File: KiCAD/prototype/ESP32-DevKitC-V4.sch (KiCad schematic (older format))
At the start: 10 parts

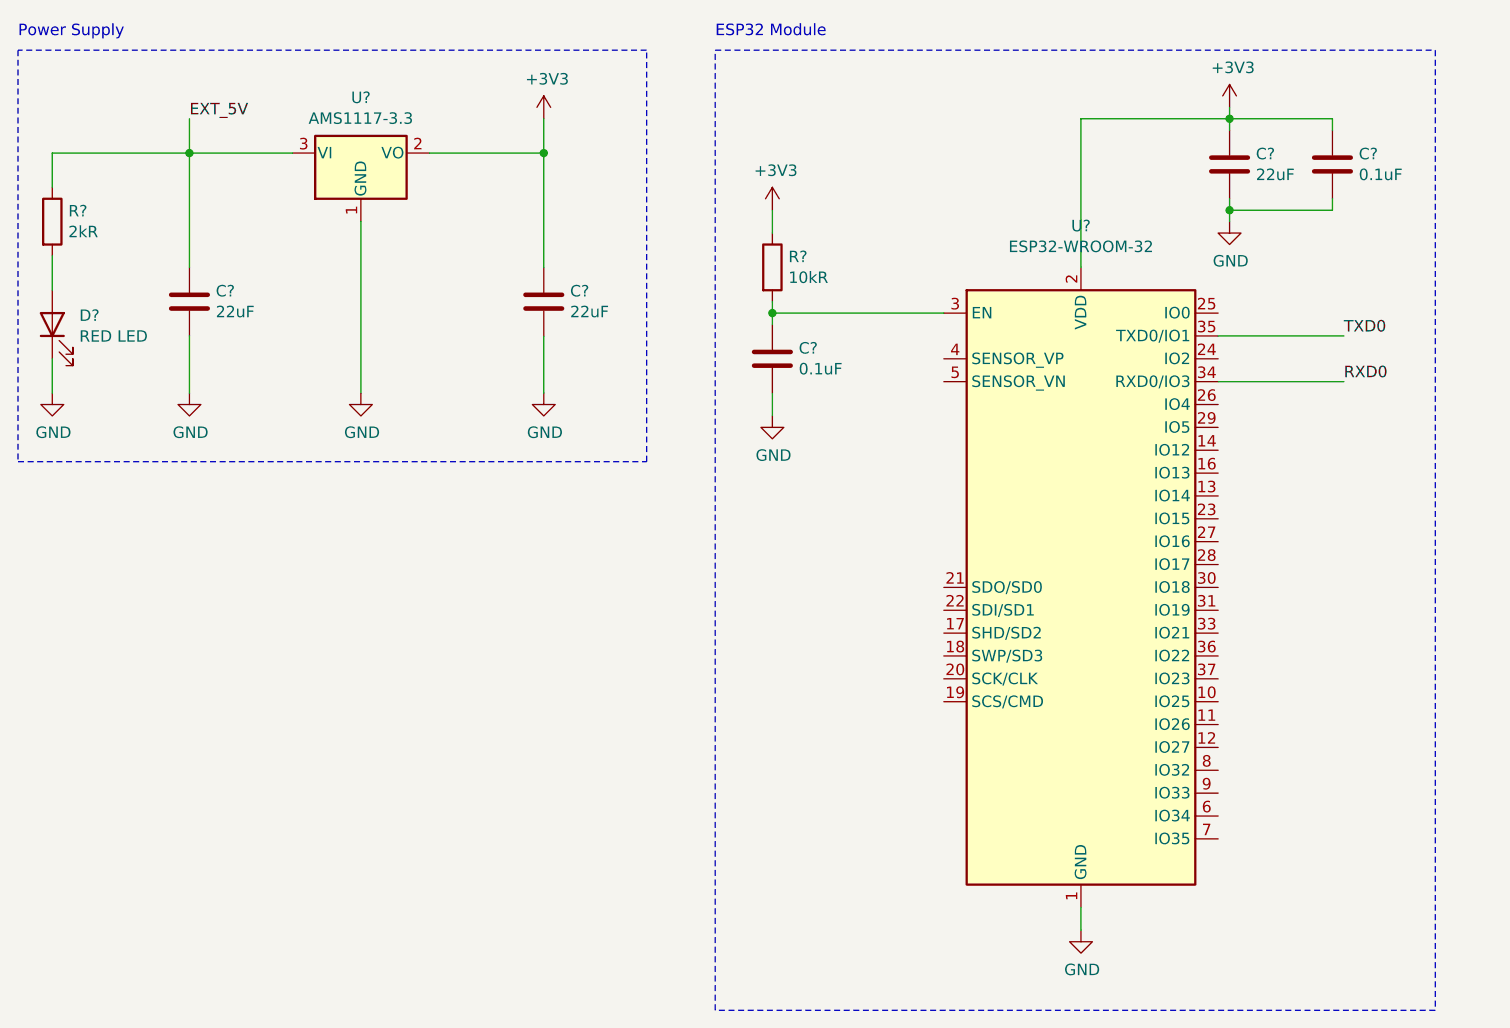
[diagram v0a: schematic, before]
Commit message: Add switch button connections
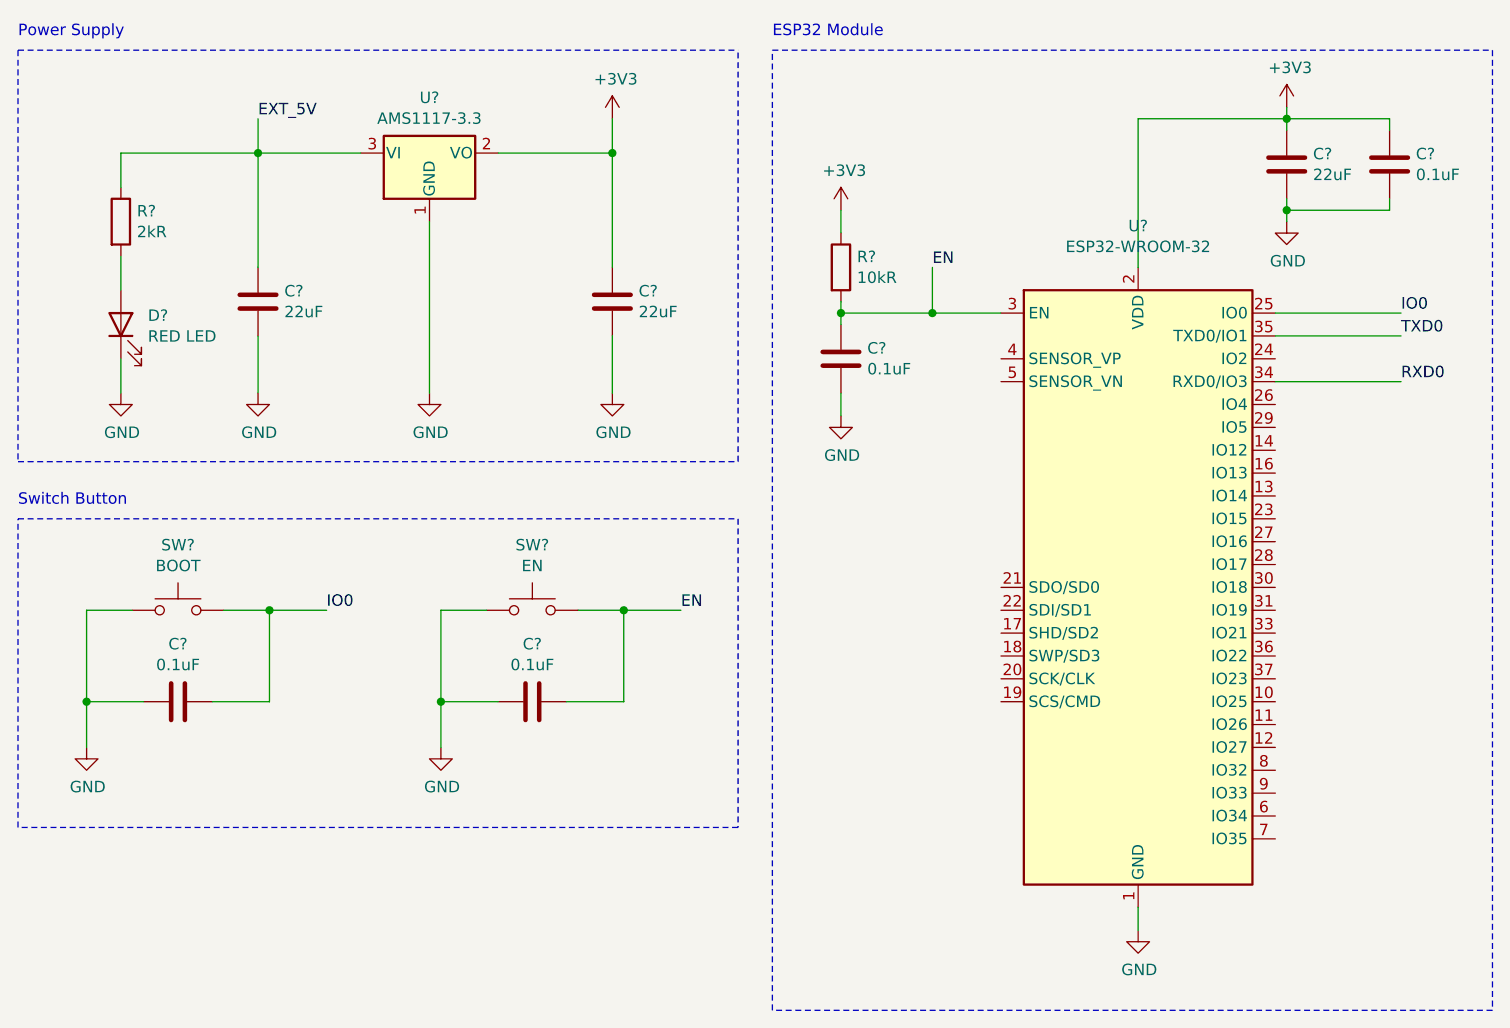
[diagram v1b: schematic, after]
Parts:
- added C? (x2): 0.1uF, symbol Device:C
- added SW?: BOOT, symbol Switch:SW_Push
- added SW?: EN, symbol Switch:SW_Push
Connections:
- net GND: now also C?.1, C?.1, SW?.1, SW?.1
- net IO0: now reaches U?.25 (IO0)
- net IO0: now also C?.2, SW?.2
- net EN: now reaches C?.1, R?.2, U?.3 (EN)
- net EN: now also C?.2, SW?.2
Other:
- note added: "Switch Button"
- moved on the sheet: C?, D?, R?, U?

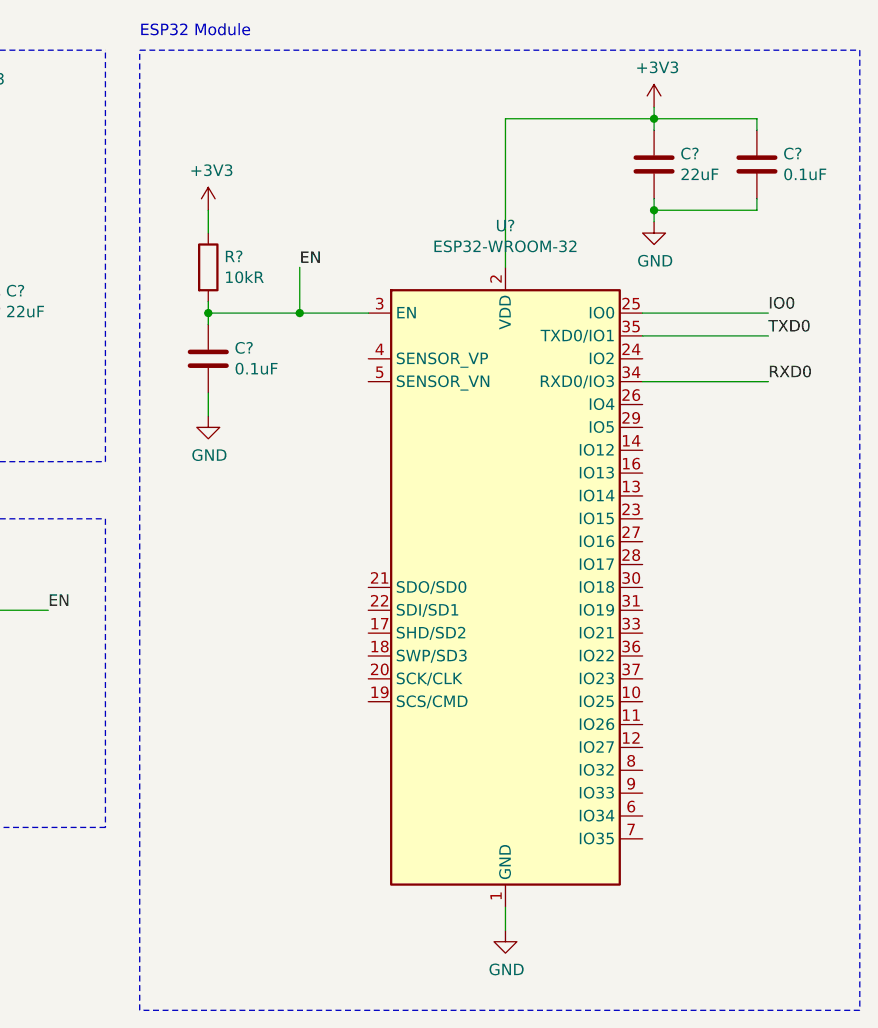
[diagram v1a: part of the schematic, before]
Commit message: Finish labels on ESP32 module
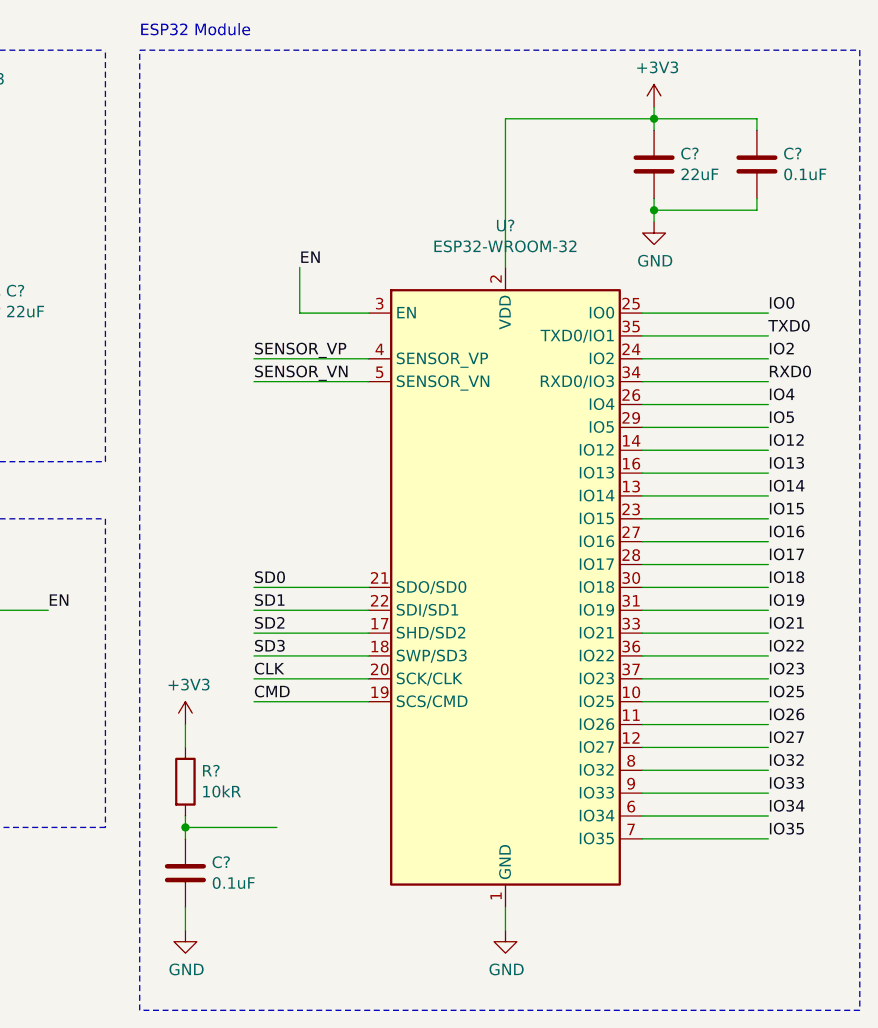
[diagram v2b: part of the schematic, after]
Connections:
- net EN: no longer C?.1, R?.2
- net IO25: now reaches U?.10 (IO25)
- net IO26: now reaches U?.11 (IO26)
- net IO27: now reaches U?.12 (IO27)
- net IO14: now reaches U?.13 (IO14)
- net IO12: now reaches U?.14 (IO12)
- net IO13: now reaches U?.16 (IO13)
- net SD2: now reaches U?.17 (SHD/SD2)
- net SD3: now reaches U?.18 (SWP/SD3)
- net CMD: now reaches U?.19 (SCS/CMD)
- net CLK: now reaches U?.20 (SCK/CLK)
- net SD0: now reaches U?.21 (SDO/SD0)
- net SD1: now reaches U?.22 (SDI/SD1)
- net IO15: now reaches U?.23 (IO15)
- net IO2: now reaches U?.24 (IO2)
- net IO4: now reaches U?.26 (IO4)
- net IO16: now reaches U?.27 (IO16)
- net IO17: now reaches U?.28 (IO17)
- net IO5: now reaches U?.29 (IO5)
- net IO18: now reaches U?.30 (IO18)
- net IO19: now reaches U?.31 (IO19)
- net IO21: now reaches U?.33 (IO21)
- net IO22: now reaches U?.36 (IO22)
- net IO23: now reaches U?.37 (IO23)
- net SENSOR_VP: now reaches U?.4 (SENSOR_VP)
- net SENSOR_VN: now reaches U?.5 (SENSOR_VN)
- net IO34: now reaches U?.6 (IO34)
- net IO35: now reaches U?.7 (IO35)
- net IO32: now reaches U?.8 (IO32)
- net IO33: now reaches U?.9 (IO33)
- new net: C?.1, R?.2
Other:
- moved on the sheet: C?, R?
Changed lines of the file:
@@
 L power:+3V3 #PWR?
 U 1 1 5F9419AA
-P 4300 1400
-F 0 "#PWR?" H 4300 1250 50  0001 C CNN
-F 1 "+3V3" H 4315 1573 50  0000 C CNN
-F 2 "" H 4300 1400 50  0001 C CNN
-F 3 "" H 4300 1400 50  0001 C CNN
-	1    4300 1400
+P 4200 3650
+F 0 "#PWR?" H 4200 3500 50  0001 C CNN
+F 1 "+3V3" H 4215 3823 50  0000 C CNN
+F 2 "" H 4200 3650 50  0001 C CNN
+F 3 "" H 4200 3650 50  0001 C CNN
+	1    4200 3650
 	1    0    0    -1
 $EndComp
@@
 L Device:R R?
 U 1 1 5F94208F
-P 4300 1650
-F 0 "R?" H 4370 1696 50  0000 L CNN
-F 1 "10kR" H 4370 1605 50  0000 L CNN
-F 2 "" V 4230 1650 50  0001 C CNN
-F 3 "~" H 4300 1650 50  0001 C CNN
-	1    4300 1650
+P 4200 3900
+F 0 "R?" H 4270 3946 50  0000 L CNN
+F 1 "10kR" H 4270 3855 50  0000 L CNN
+F 2 "" V 4130 3900 50  0001 C CNN
+F 3 "~" H 4200 3900 50  0001 C CNN
+	1    4200 3900
 	1    0    0    -1
 $EndComp
@@
 L Device:C C?
 U 1 1 5F9429EB
-P 4300 2050
-F 0 "C?" H 4415 2096 50  0000 L CNN
-F 1 "0.1uF" H 4415 2005 50  0000 L CNN
-F 2 "" H 4338 1900 50  0001 C CNN
-F 3 "~" H 4300 2050 50  0001 C CNN
-F 4 "50V" H 4415 2005 50  0001 L CNN "Voltage"
-F 5 "10%" H 4415 1914 50  0001 L CNN "Tolerance"
-	1    4300 2050
+P 4200 4300
+F 0 "C?" H 4315 4346 50  0000 L CNN
+F 1 "0.1uF" H 4315 4255 50  0000 L CNN
+F 2 "" H 4238 4150 50  0001 C CNN
+F 3 "~" H 4200 4300 50  0001 C CNN
+F 4 "50V" H 4315 4255 50  0001 L CNN "Voltage"
+F 5 "10%" H 4315 4164 50  0001 L CNN "Tolerance"
+	1    4200 4300
 	1    0    0    -1
 $EndComp
@@
 L power:GND #PWR?
 U 1 1 5F942C61
-P 4300 2300
-F 0 "#PWR?" H 4300 2050 50  0001 C CNN
-F 1 "GND" H 4305 2127 50  0000 C CNN
-F 2 "" H 4300 2300 50  0001 C CNN
-F 3 "" H 4300 2300 50  0001 C CNN
-	1    4300 2300
-	1    0    0    -1
-$EndComp
-Wire Wire Line
-	4300 2300 4300 2200
-Wire Wire Line
-	4300 1500 4300 1400
+P 4200 4550
+F 0 "#PWR?" H 4200 4300 50  0001 C CNN
+F 1 "GND" H 4205 4377 50  0000 C CNN
+F 2 "" H 4200 4550 50  0001 C CNN
+F 3 "" H 4200 4550 50  0001 C CNN
+	1    4200 4550
+	1    0    0    -1
+$EndComp
+Wire Wire Line
+	4200 4550 4200 4450
+Wire Wire Line
+	4200 3750 4200 3650
 $Comp
 L power:+3V3 #PWR?
@@
 Connection ~ 3350 3150
 Wire Wire Line
-	4300 1800 4300 1850
-Connection ~ 4300 1850
-Wire Wire Line
-	4300 1850 4300 1900
-Wire Wire Line
-	4300 1850 4700 1850
+	4200 4050 4200 4100
+Connection ~ 4200 4100
+Wire Wire Line
+	4200 4100 4200 4150
+Wire Wire Line
+	4200 4100 4600 4100
 Wire Wire Line
 	4700 1650 4700 1850
-Connection ~ 4700 1850
 Wire Wire Line
 	4700 1850 5000 1850
@@
 Wire Notes Line
 	700  2500 3850 2500
+Wire Wire Line
+	6200 2250 6750 2250
+Wire Wire Line
+	6200 2050 6750 2050
+Wire Wire Line
+	6200 2350 6750 2350
+Wire Wire Line
+	6200 2450 6750 2450
+Wire Wire Line
+	6200 2550 6750 2550
+Wire Wire Line
+	6200 2650 6750 2650
+Wire Wire Line
+	6200 2750 6750 2750
+Wire Wire Line
+	6200 2850 6750 2850
+Wire Wire Line
+	6200 2950 6750 2950
+Wire Wire Line
+	6200 3050 6750 3050
+Wire Wire Line
+	6200 3150 6750 3150
+Wire Wire Line
+	6200 3250 6750 3250
+Wire Wire Line
+	6200 3350 6750 3350
+Wire Wire Line
+	6200 3450 6750 3450
+Wire Wire Line
+	6200 3550 6750 3550
+Wire Wire Line
+	6200 3650 6750 3650
+Wire Wire Line
+	6200 3750 6750 3750
+Wire Wire Line
+	6200 3850 6750 3850
+Wire Wire Line
+	6200 3950 6750 3950
+Wire Wire Line
+	6200 4050 6750 4050
+Wire Wire Line
+	6200 4150 6750 4150
+Wire Wire Line
+	5000 3050 4500 3050
+Wire Wire Line
+	5000 3150 4500 3150
+Wire Wire Line
+	5000 3250 4500 3250
+Wire Wire Line
+	5000 3350 4500 3350
+Wire Wire Line
+	5000 3450 4500 3450
+Wire Wire Line
+	5000 3550 4500 3550
+Text Label 4500 3050 0    50   ~ 0
+SD0
+Text Label 4500 3150 0    50   ~ 0
+SD1
+Text Label 4500 3250 0    50   ~ 0
+SD2
+Text Label 4500 3350 0    50   ~ 0
+SD3
+Text Label 4500 3450 0    50   ~ 0
+CLK
+Text Label 4500 3550 0    50   ~ 0
+CMD
+Wire Wire Line
+	5000 2150 4500 2150
+Wire Wire Line
+	5000 2050 4500 2050
+Text Label 4500 2050 0    50   ~ 0
+SENSOR_VP
+Text Label 4500 2150 0    50   ~ 0
+SENSOR_VN
+Text Label 6750 2050 0    50   ~ 0
+IO2
+Text Label 6750 2250 0    50   ~ 0
+IO4
+Text Label 6750 2350 0    50   ~ 0
+IO5
+Text Label 6750 2450 0    50   ~ 0
+IO12
+Text Label 6750 2550 0    50   ~ 0
+IO13
+Text Label 6750 2650 0    50   ~ 0
+IO14
+Text Label 6750 2750 0    50   ~ 0
+IO15
+Text Label 6750 2850 0    50   ~ 0
+IO16
+Text Label 6750 2950 0    50   ~ 0
+IO17
+Text Label 6750 3050 0    50   ~ 0
+IO18
+Text Label 6750 3150 0    50   ~ 0
+IO19
+Text Label 6750 3250 0    50   ~ 0
+IO21
+Text Label 6750 3350 0    50   ~ 0
+IO22
+Text Label 6750 3450 0    50   ~ 0
+IO23
+Text Label 6750 3550 0    50   ~ 0
+IO25
+Text Label 6750 3650 0    50   ~ 0
+IO26
+Text Label 6750 3750 0    50   ~ 0
+IO27
+Text Label 6750 3850 0    50   ~ 0
+IO32
+Text Label 6750 3950 0    50   ~ 0
+IO33
+Text Label 6750 4050 0    50   ~ 0
+IO34
+Text Label 6750 4150 0    50   ~ 0
+IO35
 $EndSCHEMATC
